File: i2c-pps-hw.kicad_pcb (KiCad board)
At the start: 4 copper layers, 85 x 50 mm, 117 parts, among them J1 +5V, J2 Vout, J3 Digital I/O, Q1 SiR880BDP, Q2 SiR880BDP, Q3 SiR880BDP, Q4 SiR880BDP, Q5 SIS413DN, Q6 MMBT3904, Q7 MMBT3904, Q8 SIS413DN, U1 BQ25758S, U2 AP2210-3.3, U3 74AHC1G14

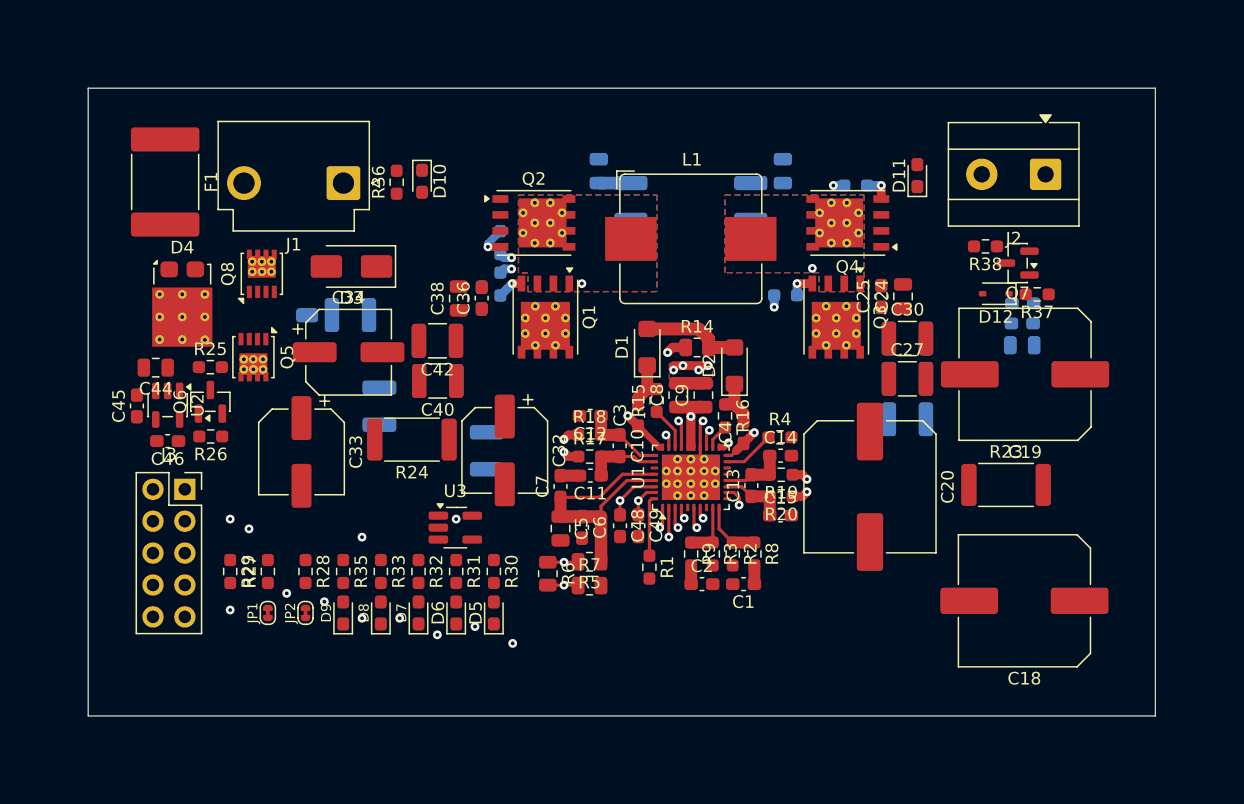
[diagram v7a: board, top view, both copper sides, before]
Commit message: Route the PCB
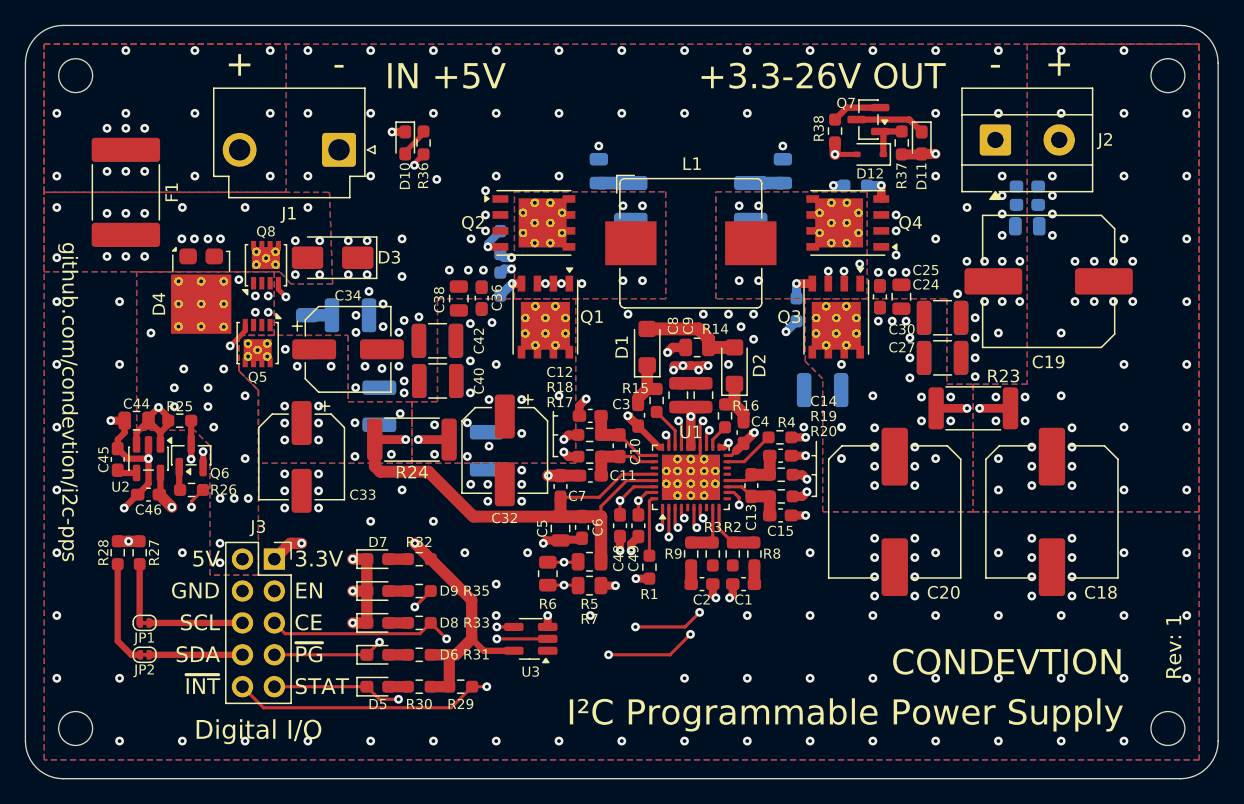
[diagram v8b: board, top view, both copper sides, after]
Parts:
- added MH1: MountingHole_2.7mm_M2.5_Guarded, i2c-pps-hw:MountingHole_2.7mm_M2.5_Guarded, F.Cu at (89.0, 77.0)
- added MH2: MountingHole_2.7mm_M2.5_Guarded, i2c-pps-hw:MountingHole_2.7mm_M2.5_Guarded, F.Cu at (176.0, 77.0)
- added MH3: MountingHole_2.7mm_M2.5_Guarded, i2c-pps-hw:MountingHole_2.7mm_M2.5_Guarded, F.Cu at (176.0, 129.0)
- added MH4: MountingHole_2.7mm_M2.5_Guarded, i2c-pps-hw:MountingHole_2.7mm_M2.5_Guarded, F.Cu at (89.0, 129.0)
- moved R29 20.5 mm to (119.7, 125.7), turned to 0 degrees
- moved Q7 16.5 mm to (152.1, 80.5)
- moved R37 16.2 mm to (154.8, 82.4), turned to 90 degrees
- moved R38 15.1 mm to (149.5, 81.4), turned to -90 degrees
- moved R28 15.0 mm to (92.3, 115.0)
- moved D12 14.9 mm to (152.3, 83.3)
- moved JP2 13.2 mm to (94.5, 123.1), turned to 180 degrees
- moved D5 10.9 mm to (113.1, 125.7), turned to 0 degrees
- moved R30 10.9 mm to (116.4, 125.7), turned to 180 degrees
- moved U3 10.7 mm to (125.2, 121.9), turned to 180 degrees
- moved R27 10.3 mm to (94.1, 115.0)
- moved JP1 9.84 mm to (94.5, 120.6), turned to 180 degrees
- moved C23 9.49 mm to (164.8, 89.0)
- moved C22 9.46 mm to (164.8, 87.3)
- moved C21 9.32 mm to (164.8, 85.8)
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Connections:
- J2 pad 1: /Controller and Power Stage/VOUT_Filtered -> GND
- J2 pad 2: GND -> /Controller and Power Stage/VOUT_Filtered
- J3 pad 10: /Controller and Power Stage/~{PG} -> /Controller and Power Stage/~{INT}
- J3 pad 3: GND -> /Digital IO and Indication/EN
- J3 pad 4: /Digital IO and Indication/EN -> GND
- J3 pad 5: /Controller and Power Stage/SCL -> /Digital IO and Indication/CE
- J3 pad 6: /Digital IO and Indication/CE -> /Controller and Power Stage/SCL
- J3 pad 7: /Controller and Power Stage/SDA -> /Controller and Power Stage/~{PG}
- J3 pad 8: /Controller and Power Stage/~{INT} -> /Controller and Power Stage/SDA
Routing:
- net /Controller and Power Stage/VOUT_Filtered: track 2.99 -> 98.0 mm, vias 2 -> 47
- net /Digital IO and Indication/3.3v: track 0.00 -> 52.4 mm, vias 2 -> 4
- net /Controller and Power Stage/SCL: track 1.71 -> 52.9 mm, vias 2 -> 1
- net /Controller and Power Stage/SDA: track 2.35 -> 52.8 mm, vias 2 -> 1
- net /Controller and Power Stage/~{INT}: track 1.69 -> 47.6 mm
- net /Controller and Power Stage/STAT: track 0.94 -> 45.5 mm
- net GND: track 9.30 -> 53.3 mm, vias 7 -> 204
- net /Controller and Power Stage/~{PG}: track 1.69 -> 45.2 mm, vias 2 -> 4
- net /Controller and Power Stage/+5V_Run: track 23.8 -> 60.0 mm, vias 1 -> 15
- net /Digital IO and Indication/+5V_Prot: track 0.00 -> 30.5 mm, vias 0 -> 22
- net /Digital IO and Indication/EN: track 0.00 -> 28.0 mm, vias 1 -> 2
- net /Controller and Power Stage/~{CE}: track 0.94 -> 26.8 mm, vias 2 -> 4
- net /Digital IO and Indication/CE: track 0.00 -> 23.0 mm, vias 1 -> 2
- net /Controller and Power Stage/VOUT_Switcher: track 1.29 -> 22.9 mm, vias 1 -> 24
- net /Controller and Power Stage/+5V_Filtered: track 1.29 -> 18.2 mm, vias 1 -> 16
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- added copper zone on B.Cu, net /Controller and Power Stage/+5V_Filtered
- added copper zone on F.Cu, net /Controller and Power Stage/+5V_Filtered
- added copper zone on In2.Cu, net /Controller and Power Stage/+5V_Filtered
- added copper zone on B.Cu, net /Controller and Power Stage/+5V_Run
- added copper zone on F.Cu, net /Controller and Power Stage/+5V_Run
- added copper zone on In2.Cu, net /Controller and Power Stage/+5V_Run
- added copper zone on In2.Cu, net /Controller and Power Stage/SW1
- added copper zone on In2.Cu, net /Controller and Power Stage/SW2
- added copper zone on B.Cu, net /Controller and Power Stage/VOUT_Filtered
- added copper zone on F.Cu, net /Controller and Power Stage/VOUT_Filtered
- added copper zone on In2.Cu, net /Controller and Power Stage/VOUT_Filtered
- added copper zone on B.Cu, net /Controller and Power Stage/VOUT_Switcher
- added copper zone on F.Cu, net /Controller and Power Stage/VOUT_Switcher
- added copper zone on In2.Cu, net /Controller and Power Stage/VOUT_Switcher
- added copper zone on B.Cu, net /Digital IO and Indication/+5V_Prot
- added copper zone on F.Cu, net /Digital IO and Indication/+5V_Prot
- added copper zone on In2.Cu, net /Digital IO and Indication/+5V_Prot
- added copper zone on B.Cu, net /Master Switch/+5V
- added copper zone on F.Cu, net /Master Switch/+5V
- added copper zone on In2.Cu, net /Master Switch/+5V
- added copper zone on B.Cu, net GND
- added copper zone on In1.Cu, net GND
- added copper zone on In2.Cu, net GND
- added copper zone on B.Cu, net Net-(D3-A2)
- added copper zone on F.Cu, net Net-(D3-A2)
- added copper zone on In2.Cu, net Net-(D3-A2)
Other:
- board size 85 x 50 mm -> 95 x 60 mm
- board text added: "+"
- board text added: "+3.3-26V OUT"
- board text added: "-"
- board text added: "3.3V"
- board text added: "5V"
- board text added: "CE"
- board text added: "CONDEVTION"
- board text added: "Digital I/O"
- board text added: "EN"
- board text added: "GND"
- board text added: "IN +5V"
- board text added: "I²C Programmable Power Supply"
- board text added: "Rev: ${REVISION}"
- board text added: "SCL"
- board text added: "SDA"
- board text added: "STAT"
- board text added: "github.com/condevtion/i2c-pps"
- board text added: "~{INT}"
- board text added: "~{PG}"
